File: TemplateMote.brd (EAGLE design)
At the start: 34.7 x 23.1 mm, 3 parts

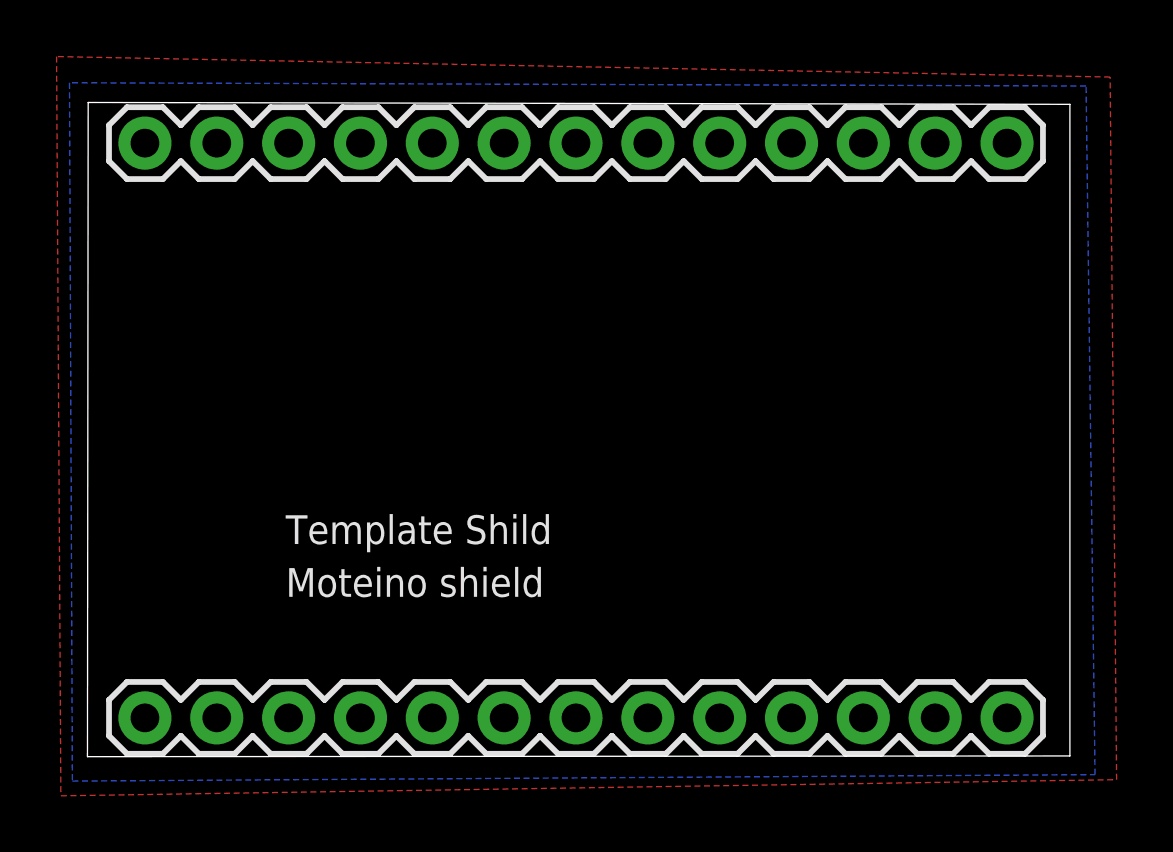
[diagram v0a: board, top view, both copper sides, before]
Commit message: fixed board shape
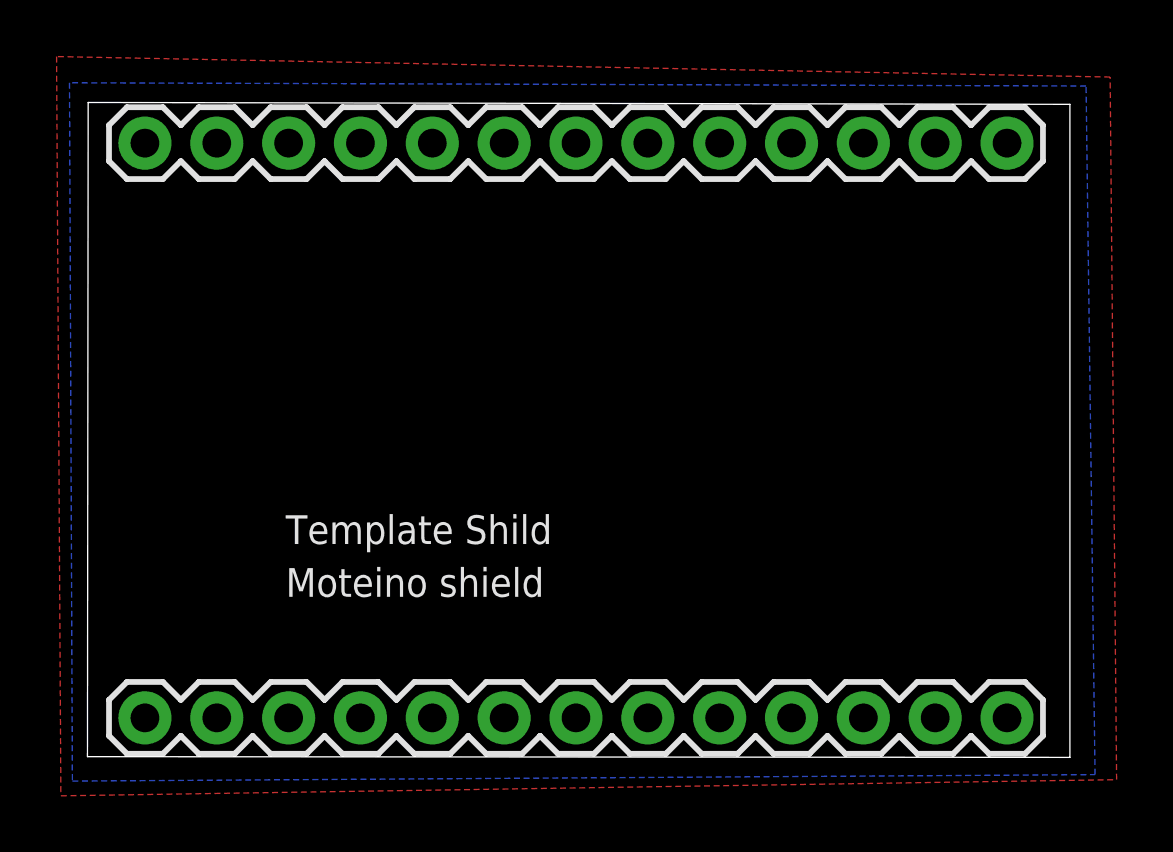
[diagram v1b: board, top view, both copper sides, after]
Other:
- board size 34.7 x 23.1 mm -> 34.7 x 23.2 mm
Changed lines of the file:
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@@
 <board>
 <plain>
-<wire x1="0.508" y1="1.1684" x2="35.2427" y2="1.1938" width="0" layer="20"/>
-<wire x1="35.2427" y1="1.1938" x2="35.2427" y2="24.2316" width="0" layer="20"/>
+<wire x1="0.508" y1="1.1684" x2="35.2427" y2="1.143" width="0" layer="20"/>
+<wire x1="35.2427" y1="1.143" x2="35.2427" y2="24.2316" width="0" layer="20"/>
 <wire x1="35.2427" y1="24.2316" x2="0.5334" y2="24.2978" width="0" layer="20"/>
 <wire x1="0.5334" y1="24.2978" x2="0.508" y2="1.1684" width="0" layer="20"/>

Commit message: fixed board shape
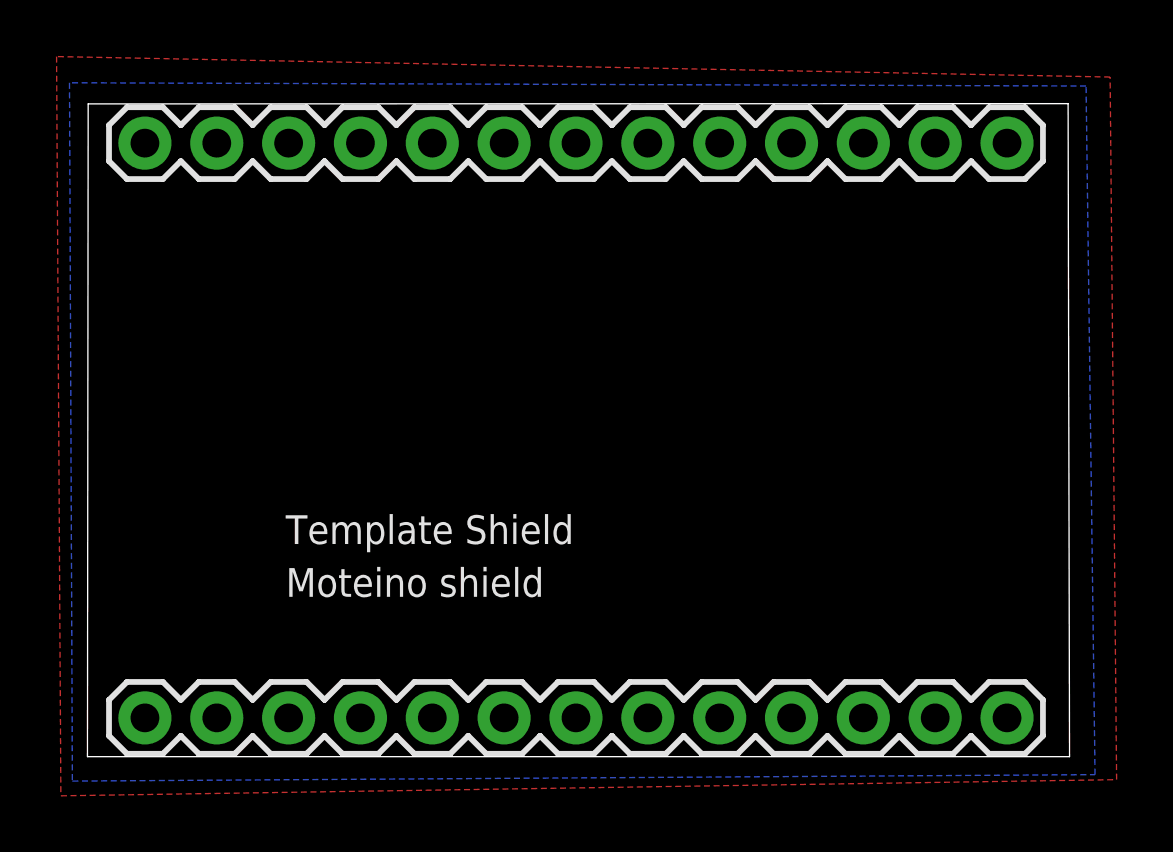
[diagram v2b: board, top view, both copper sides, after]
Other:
- board size 34.7 x 23.2 mm -> 34.7 x 23.1 mm
- board text added: "Template Shield"
- board text removed: "Template Shild"
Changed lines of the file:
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@@
 <board>
 <plain>
-<wire x1="0.508" y1="1.1684" x2="35.2427" y2="1.143" width="0" layer="20"/>
-<wire x1="35.2427" y1="1.143" x2="35.2427" y2="24.2316" width="0" layer="20"/>
-<wire x1="35.2427" y1="24.2316" x2="0.5334" y2="24.2978" width="0" layer="20"/>
-<wire x1="0.5334" y1="24.2978" x2="0.508" y2="1.1684" width="0" layer="20"/>
+<wire x1="0.508" y1="1.1684" x2="35.2298" y2="1.1684" width="0" layer="20"/>
+<wire x1="35.2298" y1="1.1684" x2="35.179" y2="24.257" width="0" layer="20"/>
+<wire x1="35.179" y1="24.257" x2="0.5334" y2="24.247" width="0" layer="20"/>
+<wire x1="0.5334" y1="24.247" x2="0.508" y2="1.1684" width="0" layer="20"/>
 <text x="7.5184" y="6.8199" size="1.016" layer="25">Moteino shield</text>
-<text x="7.5184" y="8.6868" size="1.016" layer="25">Template Shild</text>
+<text x="7.5184" y="8.6868" size="1.016" layer="25">Template Shield</text>
 </plain>
 <attributes>
